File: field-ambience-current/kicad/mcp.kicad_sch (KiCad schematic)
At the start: 48 parts, among them SW10 Modifier CLEAR (12x12x7.3 SMD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, SW6 Modifier SHIFT (12x12x7.3 SMD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, SW7 Modifier HOLD (12x12x7.3 SMD-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, SW8 Modifier DRONE (12x12x7.3 SMD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, SW9 Modifier GENERATE (12x12x7.3 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, U2 MCP23017-E/SS (I/O-Expander), U6 PCA9685PW (16-Ch I²C PWM LED-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

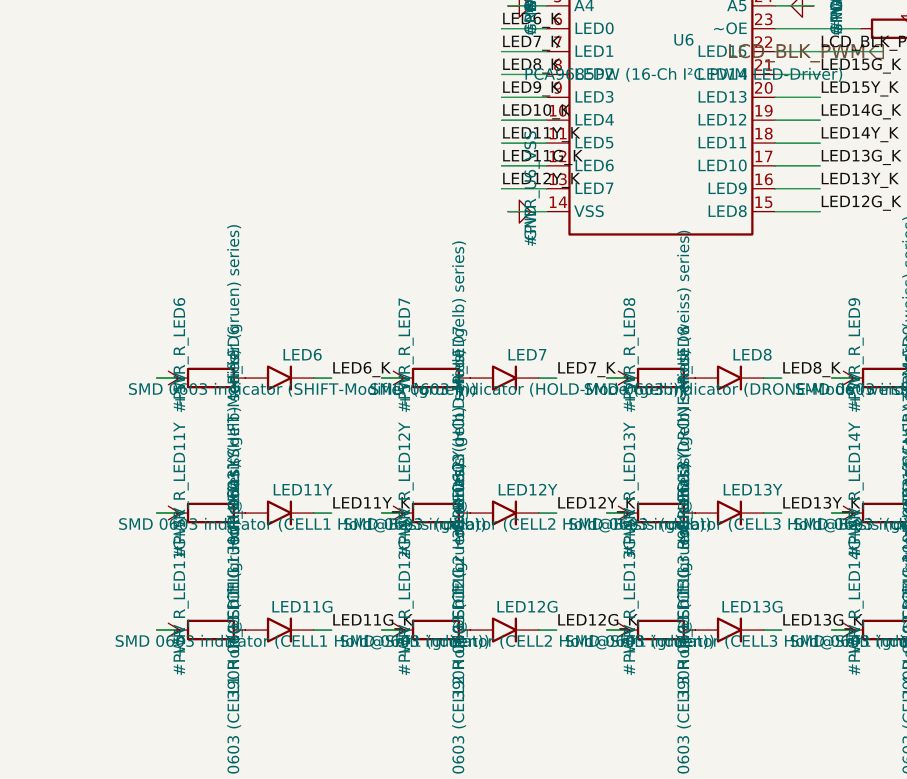
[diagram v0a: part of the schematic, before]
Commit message: docs(pcb): completeness package — pinmap, JLC BOM export, handoff doc
Make the PCB design data component- and connectivity-complete so a PCB
engineer knows every pin / net / module without re-deriving from the
generator. Closes the gaps from the hardware gap analysis: the BOM alone
isn't production-ready, the generator is the source of truth, and the
pinmap / machine BOM / handoff package were missing.

New deliverables:
- docs/hardware/PINMAP.md — every STM32H743 LQFP-100 pin (all 100) → net →
  function/AF → module → external-component pin, plus per-module net tables
  (source → all sinks) for Power/MCU/LCD/MCP+LEDs/Encoders/Audio/Battery,
  and the verified free-pin list. Distilled from the generator NETS table.
- kicad/export_jlc_bom.py — stdlib-only JLC BOM exporter; parses the 7
  generated leaf .kicad_sch, skips #PWR + DNP, groups by LCSC, quotes
  comma-bearing values. Parts without LCSC go to a stderr NO-LCSC list
  (no guessing). Prints that CPL needs a routed .kicad_pcb (doesn't exist).
- kicad/jlc_bom.csv — generated: 57 LCSC parts, 188 placements.
- docs/hardware/PCB_HANDOFF.md — what's in the package, the engineer
  workflow, and the hard blockers before a fab order (ERC in GUI, layout +
  routing, mechanical coords, Gerber/CPL — all KiCad-GUI / user-side since
  there is no kicad-cli in this env).

Generator: swap LED6/LED7 physical colors to spec — Shift = gelb (C2287),
Hold = gruen (C12624) — attribute-only (same footprint/pads/net), so the
schematic, BOM and firmware are now consistent. Regenerated mcp.kicad_sch.

Also: PROJECT_STATUS r18.64 (1.9" display freeze, per-world musical
identity, Echo/Blur); MECHANICAL_REQUIREMENTS 1.9" freeze line;
component_reviews/README F-1/F-2/F-3 status corrections.

Docs/kicad/tools only — outside the firmware CI path filter.

Co-Authored-By: Claude Opus 4.8 <noreply@anthropic.com>
Claude-Session: https://claude.ai/code/session_01K5kLTFpDCCoYwx2dq6RkAv
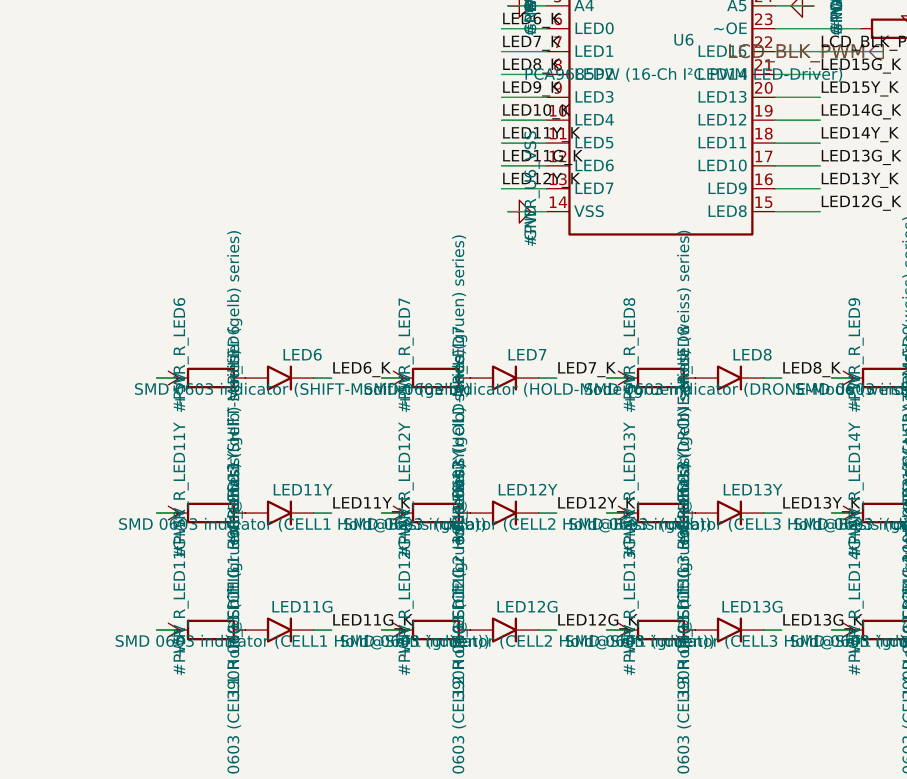
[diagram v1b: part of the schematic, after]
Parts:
- LED6: value SMD 0603 indicator (SHIFT-Modifier (gruen)) -> SMD 0603 indicator (SHIFT-Modifier (gelb)); LCSC C12624 -> C2287; MPN KT-0603G (Hubei KENTO, pure green 525nm 0603, Vf 3.1V) -> KT-0603Y (Hubei KENTO, yellow 0603, Vf 2.4V)
- LED7: value SMD 0603 indicator (HOLD-Mode (gelb)) -> SMD 0603 indicator (HOLD-Mode (gruen)); LCSC C2287 -> C12624; MPN KT-0603Y (Hubei KENTO, yellow 0603, Vf 2.4V) -> KT-0603G (Hubei KENTO, pure green 525nm 0603, Vf 3.1V)
- R_LED6: value 390R 0603 (SHIFT-Modifier (gruen) series) -> 390R 0603 (SHIFT-Modifier (gelb) series)
- R_LED7: value 390R 0603 (HOLD-Mode (gelb) series) -> 390R 0603 (HOLD-Mode (gruen) series)
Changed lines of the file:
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@@
       (property "Reference" "R_LED6" (at 82.54 197.46 0)
         (effects (font (size 1.27 1.27))))
-      (property "Value" "390R 0603 (SHIFT-Modifier (gruen) series)" (at 82.54 201.27 0)
+      (property "Value" "390R 0603 (SHIFT-Modifier (gelb) series)" (at 82.54 201.27 0)
         (effects (font (size 1.27 1.27))))
       (property "Footprint" "Resistor_SMD:R_0603_1608Metric" (at 80 200 0)
@@
       (property "Reference" "LED6" (at 90.16000000000001 197.46 0)
         (effects (font (size 1.27 1.27))))
-      (property "Value" "SMD 0603 indicator (SHIFT-Modifier (gruen))" (at 90.16000000000001 201.27 0)
+      (property "Value" "SMD 0603 indicator (SHIFT-Modifier (gelb))" (at 90.16000000000001 201.27 0)
         (effects (font (size 1.27 1.27))))
       (property "Footprint" "LED_SMD:LED_0603_1608Metric" (at 87.62 200 0)
@@
       (property "Datasheet" "~" (at 87.62 200 0)
         (effects (font (size 1.27 1.27)) hide))
-      (property "MPN" "KT-0603G (Hubei KENTO, pure green 525nm 0603, Vf 3.1V)" (at 90.16000000000001 203.81 0)
+      (property "MPN" "KT-0603Y (Hubei KENTO, yellow 0603, Vf 2.4V)" (at 90.16000000000001 203.81 0)
         (effects (font (size 1.27 1.27)) hide))
-      (property "LCSC" "C12624" (at 90.16000000000001 205.08 0)
+      (property "LCSC" "C2287" (at 90.16000000000001 205.08 0)
         (effects (font (size 1.27 1.27)) hide))
     (instances
@@
       (property "Reference" "R_LED7" (at 107.54 197.46 0)
         (effects (font (size 1.27 1.27))))
-      (property "Value" "390R 0603 (HOLD-Mode (gelb) series)" (at 107.54 201.27 0)
+      (property "Value" "390R 0603 (HOLD-Mode (gruen) series)" (at 107.54 201.27 0)
         (effects (font (size 1.27 1.27))))
       (property "Footprint" "Resistor_SMD:R_0603_1608Metric" (at 105 200 0)
@@
       (property "Reference" "LED7" (at 115.16000000000001 197.46 0)
         (effects (font (size 1.27 1.27))))
-      (property "Value" "SMD 0603 indicator (HOLD-Mode (gelb))" (at 115.16000000000001 201.27 0)
+      (property "Value" "SMD 0603 indicator (HOLD-Mode (gruen))" (at 115.16000000000001 201.27 0)
         (effects (font (size 1.27 1.27))))
       (property "Footprint" "LED_SMD:LED_0603_1608Metric" (at 112.62 200 0)
@@
       (property "Datasheet" "~" (at 112.62 200 0)
         (effects (font (size 1.27 1.27)) hide))
-      (property "MPN" "KT-0603Y (Hubei KENTO, yellow 0603, Vf 2.4V)" (at 115.16000000000001 203.81 0)
+      (property "MPN" "KT-0603G (Hubei KENTO, pure green 525nm 0603, Vf 3.1V)" (at 115.16000000000001 203.81 0)
         (effects (font (size 1.27 1.27)) hide))
-      (property "LCSC" "C2287" (at 115.16000000000001 205.08 0)
+      (property "LCSC" "C12624" (at 115.16000000000001 205.08 0)
         (effects (font (size 1.27 1.27)) hide))
     (instances

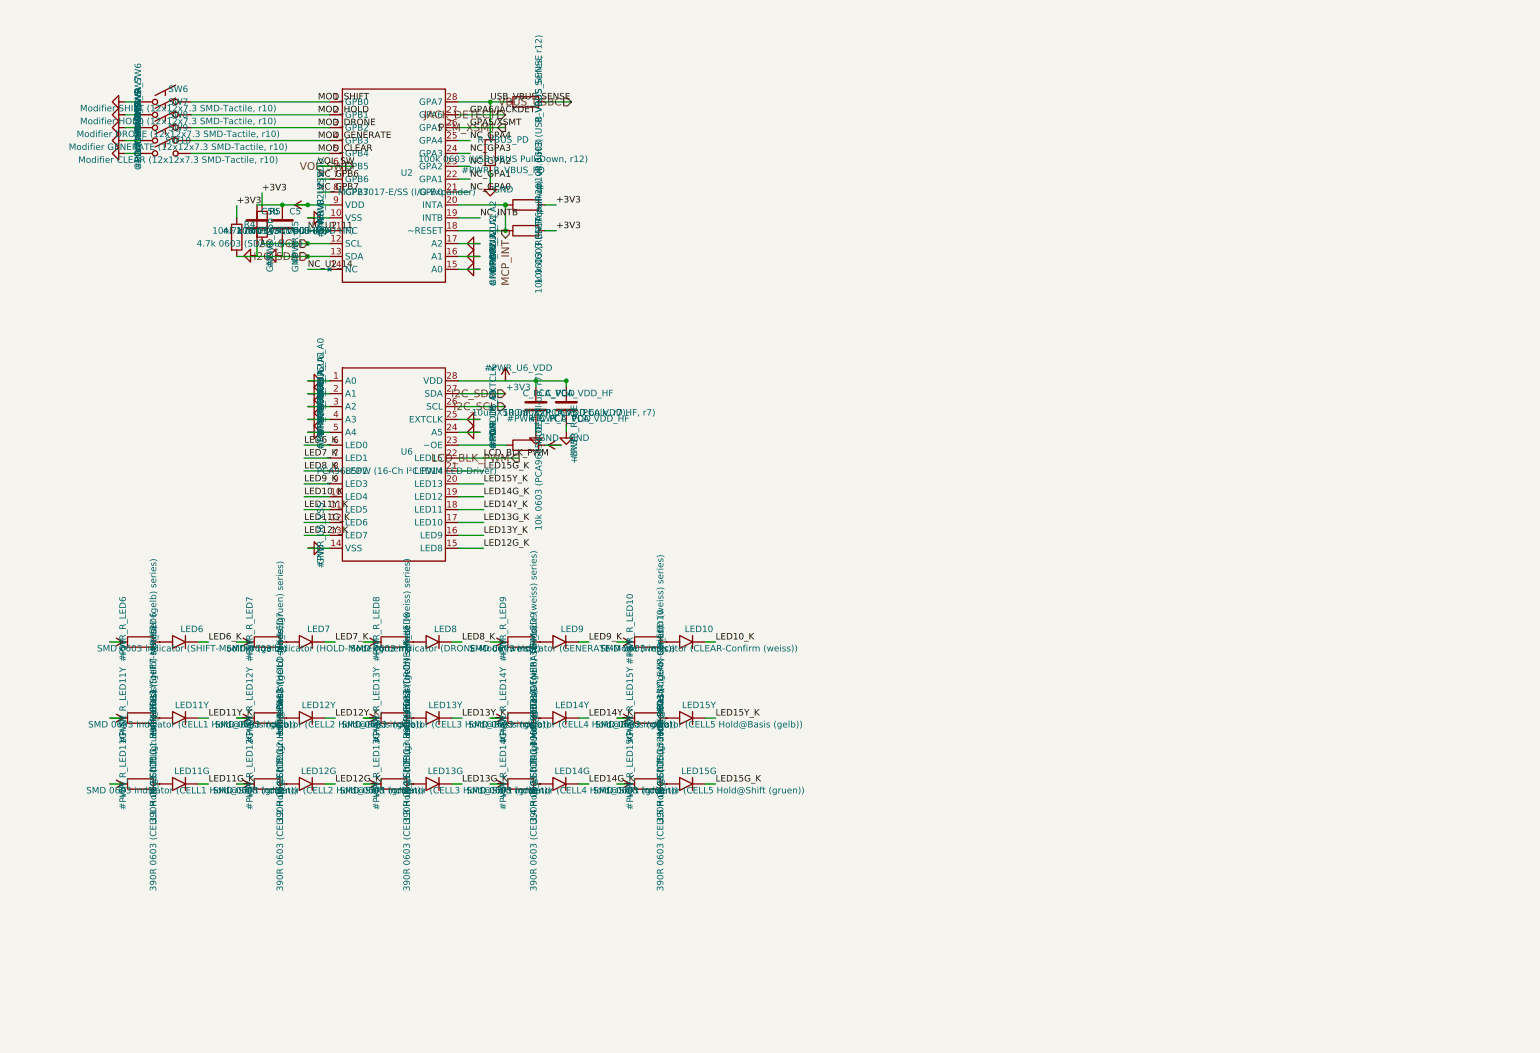
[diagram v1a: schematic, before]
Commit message: feat(pcb): live level-meter — 2nd PCA9685 (U10) → 8 VU LEDs (OP-1 style) (#66)
* docs(pcb): completeness package — pinmap, JLC BOM export, handoff doc

Make the PCB design data component- and connectivity-complete so a PCB
engineer knows every pin / net / module without re-deriving from the
generator. Closes the gaps from the hardware gap analysis: the BOM alone
isn't production-ready, the generator is the source of truth, and the
pinmap / machine BOM / handoff package were missing.

New deliverables:
- docs/hardware/PINMAP.md — every STM32H743 LQFP-100 pin (all 100) → net →
  function/AF → module → external-component pin, plus per-module net tables
  (source → all sinks) for Power/MCU/LCD/MCP+LEDs/Encoders/Audio/Battery,
  and the verified free-pin list. Distilled from the generator NETS table.
- kicad/export_jlc_bom.py — stdlib-only JLC BOM exporter; parses the 7
  generated leaf .kicad_sch, skips #PWR + DNP, groups by LCSC, quotes
  comma-bearing values. Parts without LCSC go to a stderr NO-LCSC list
  (no guessing). Prints that CPL needs a routed .kicad_pcb (doesn't exist).
- kicad/jlc_bom.csv — generated: 57 LCSC parts, 188 placements.
- docs/hardware/PCB_HANDOFF.md — what's in the package, the engineer
  workflow, and the hard blockers before a fab order (ERC in GUI, layout +
  routing, mechanical coords, Gerber/CPL — all KiCad-GUI / user-side since
  there is no kicad-cli in this env).

Generator: swap LED6/LED7 physical colors to spec — Shift = gelb (C2287),
Hold = gruen (C12624) — attribute-only (same footprint/pads/net), so the
schematic, BOM and firmware are now consistent. Regenerated mcp.kicad_sch.

Also: PROJECT_STATUS r18.64 (1.9" display freeze, per-world musical
identity, Echo/Blur); MECHANICAL_REQUIREMENTS 1.9" freeze line;
component_reviews/README F-1/F-2/F-3 status corrections.

Docs/kicad/tools only — outside the firmware CI path filter.

Co-Authored-By: Claude Opus 4.8 <noreply@anthropic.com>
Claude-Session: https://claude.ai/code/session_01K5k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
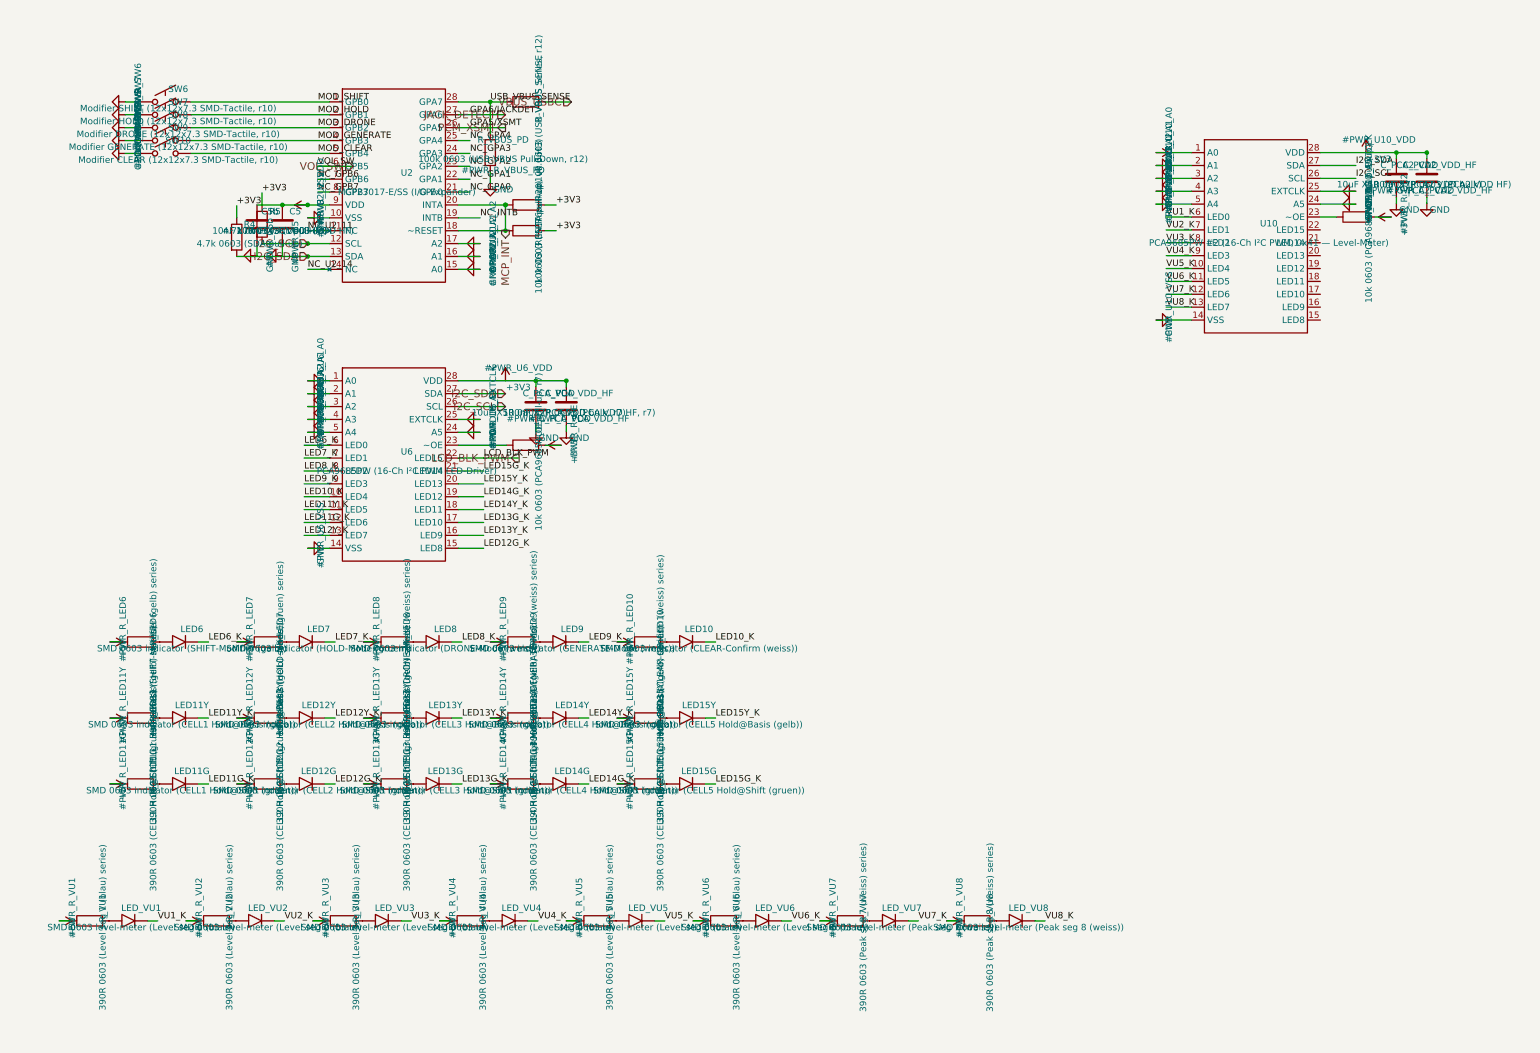
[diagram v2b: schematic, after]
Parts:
- added C_PCA2_VDD: 10uF X5R 0805 (PCA2 VDD bulk), Capacitor_SMD:C_0805_2012Metric, symbol Device:C
- added C_PCA2_VDD_HF: 100nF X7R 0603 (PCA2 VDD HF), Capacitor_SMD:C_0603_1608Metric, symbol Device:C
- added LED_VU1: SMD 0603 level-meter (Level seg 1 (blau)), LED_SMD:LED_0603_1608Metric, symbol Device:LED
- added LED_VU2: SMD 0603 level-meter (Level seg 2 (blau)), LED_SMD:LED_0603_1608Metric, symbol Device:LED
- added LED_VU3: SMD 0603 level-meter (Level seg 3 (blau)), LED_SMD:LED_0603_1608Metric, symbol Device:LED
- added LED_VU4: SMD 0603 level-meter (Level seg 4 (blau)), LED_SMD:LED_0603_1608Metric, symbol Device:LED
- added LED_VU5: SMD 0603 level-meter (Level seg 5 (blau)), LED_SMD:LED_0603_1608Metric, symbol Device:LED
- added LED_VU6: SMD 0603 level-meter (Level seg 6 (blau)), LED_SMD:LED_0603_1608Metric, symbol Device:LED
- added LED_VU7: SMD 0603 level-meter (Peak seg 7 (weiss)), LED_SMD:LED_0603_1608Metric, symbol Device:LED
- added LED_VU8: SMD 0603 level-meter (Peak seg 8 (weiss)), LED_SMD:LED_0603_1608Metric, symbol Device:LED
- added R_OE2: 10k 0603 (PCA9685 #2 /OE pull-up), Resistor_SMD:R_0603_1608Metric, symbol Device:R
- added R_VU1: 390R 0603 (Level seg 1 (blau) series), Resistor_SMD:R_0603_1608Metric, symbol Device:R
- added R_VU2: 390R 0603 (Level seg 2 (blau) series), Resistor_SMD:R_0603_1608Metric, symbol Device:R
- added R_VU3: 390R 0603 (Level seg 3 (blau) series), Resistor_SMD:R_0603_1608Metric, symbol Device:R
- added R_VU4: 390R 0603 (Level seg 4 (blau) series), Resistor_SMD:R_0603_1608Metric, symbol Device:R
- added R_VU5: 390R 0603 (Level seg 5 (blau) series), Resistor_SMD:R_0603_1608Metric, symbol Device:R
- added R_VU6: 390R 0603 (Level seg 6 (blau) series), Resistor_SMD:R_0603_1608Metric, symbol Device:R
- added R_VU7: 390R 0603 (Peak seg 7 (weiss) series), Resistor_SMD:R_0603_1608Metric, symbol Device:R
- added R_VU8: 390R 0603 (Peak seg 8 (weiss) series), Resistor_SMD:R_0603_1608Metric, symbol Device:R
- added U10: PCA9685PW #2 (16-Ch I²C PWM, 0x41 — Level-Meter), Package_SO:TSSOP-28_4.4x9.7mm_P0.65mm, symbol Driver_LED:PCA9685PW
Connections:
- net +3V3: now also C_PCA2_VDD.1, C_PCA2_VDD_HF.1, R_OE2.2, U10.1 (A0), U10.28 (VDD)
- net +5V: now also R_VU1.1, R_VU2.1, R_VU3.1, R_VU4.1, R_VU5.1, R_VU6.1, R_VU7.1, R_VU8.1
- net GND: now also C_PCA2_VDD.2, C_PCA2_VDD_HF.2, U10.14 (VSS), U10.2 (A1), U10.24 (A5), U10.25 (EXTCLK), U10.3 (A2), U10.4 (A3), U10.5 (A4)
- net I2C_SCL: now also U10.26 (SCL)
- net I2C_SDA: now also U10.27 (SDA)
- new net: LED_VU3.2 (A), R_VU3.2
- new net: LED_VU6.2 (A), R_VU6.2
- new net: LED_VU7.2 (A), R_VU7.2
- new net: LED_VU2.2 (A), R_VU2.2
- new net: LED_VU8.2 (A), R_VU8.2
- new net: LED_VU1.2 (A), R_VU1.2
- new net: R_OE2.1, U10.23 (~OE)
- new net: LED_VU5.2 (A), R_VU5.2
- new net: LED_VU4.2 (A), R_VU4.2
- new net VU1_K: LED_VU1.1 (K), U10.6 (LED0)
- new net VU2_K: LED_VU2.1 (K), U10.7 (LED1)
- new net VU3_K: LED_VU3.1 (K), U10.8 (LED2)
- new net VU4_K: LED_VU4.1 (K), U10.9 (LED3)
- new net VU5_K: LED_VU5.1 (K), U10.10 (LED4)
- new net VU6_K: LED_VU6.1 (K), U10.11 (LED5)
- new net VU7_K: LED_VU7.1 (K), U10.12 (LED6)
- new net VU8_K: LED_VU8.1 (K), U10.13 (LED7)
